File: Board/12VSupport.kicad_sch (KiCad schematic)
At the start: 33 parts, among them J1 12V, J2 BATT, J3 BUCK_IN, J4 BUCK_OUT, J5 BOOST_IN, J6 BOOST_OUT, J8 HEATER, K1 SLA-05VDC-SL-C, K2 SLA-05VDC-SL-C, K3 SLA-05VDC-SL-C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

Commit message: Change fuse holders.
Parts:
- F1, F2: footprint Fuse:Fuseholder_Blade_Mini_Keystone_3568 -> spetry:Fuseholder_Blade
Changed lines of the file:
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@@
 			)
 		)
-		(property "Footprint" "Fuse:Fuseholder_Blade_Mini_Keystone_3568"
+		(property "Footprint" "spetry:Fuseholder_Blade"
 			(at 44.45 154.178 90)
 			(effects
@@
 			)
 		)
-		(property "Footprint" "Fuse:Fuseholder_Blade_Mini_Keystone_3568"
+		(property "Footprint" "spetry:Fuseholder_Blade"
 			(at 54.61 122.682 90)
 			(effects

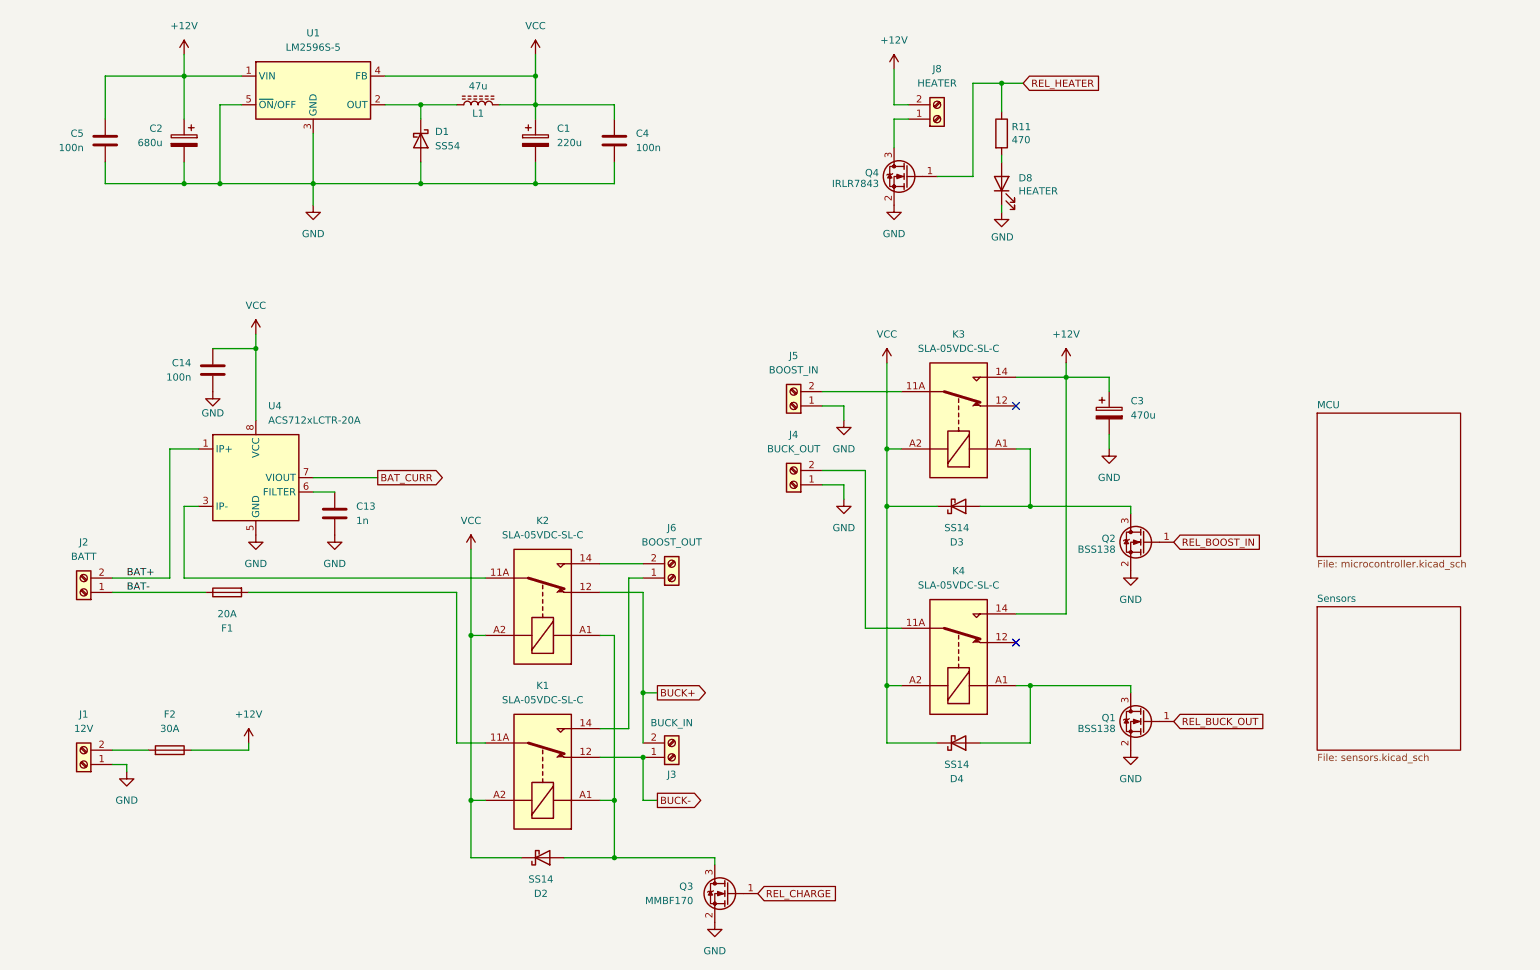
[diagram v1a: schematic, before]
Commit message: Remove diode in MCU supply line so MCU has full 5V.
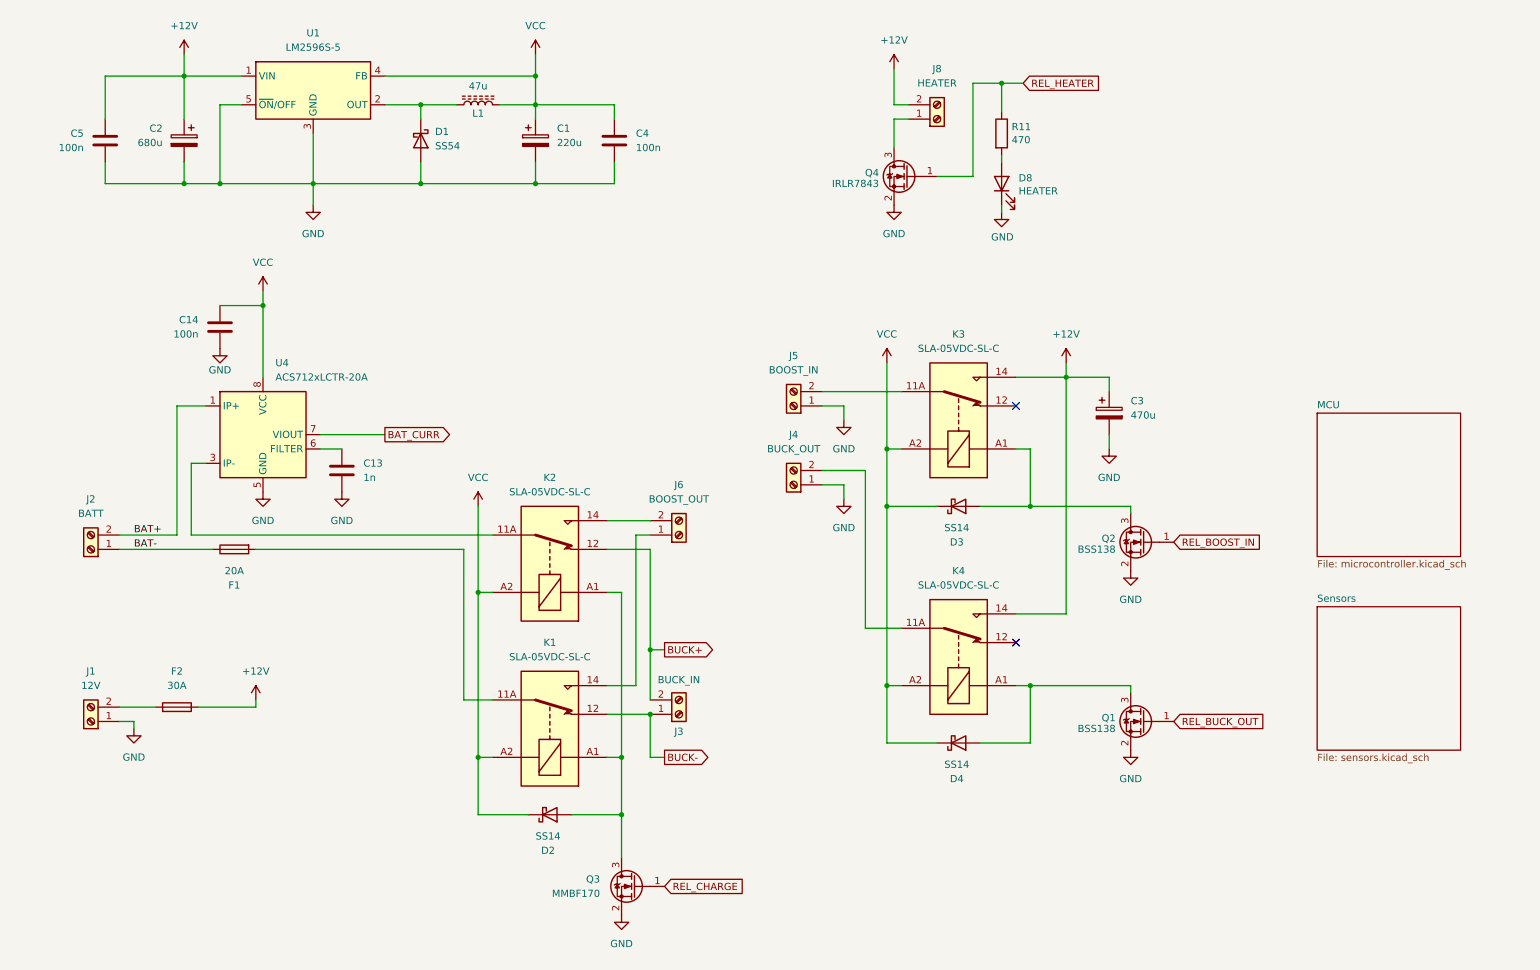
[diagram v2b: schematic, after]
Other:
- moved on the sheet: C13, C14, D2, F1, F2, J1, J2, J3, J6, K1, K2, Q3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

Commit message: Board WIP
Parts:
- F2: value 30A -> 40A
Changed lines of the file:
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@@
 			)
 		)
-		(property "Value" "30A"
+		(property "Value" "40A"
 			(at 45.72 140.97 90)
 			(effects

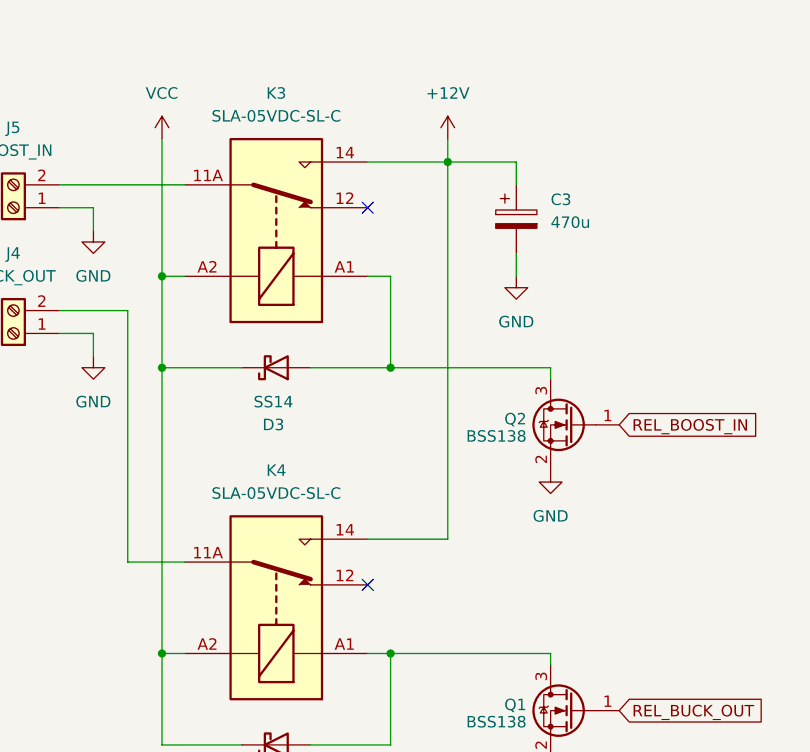
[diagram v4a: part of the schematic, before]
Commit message: Layout improvements. Set version to 1.1
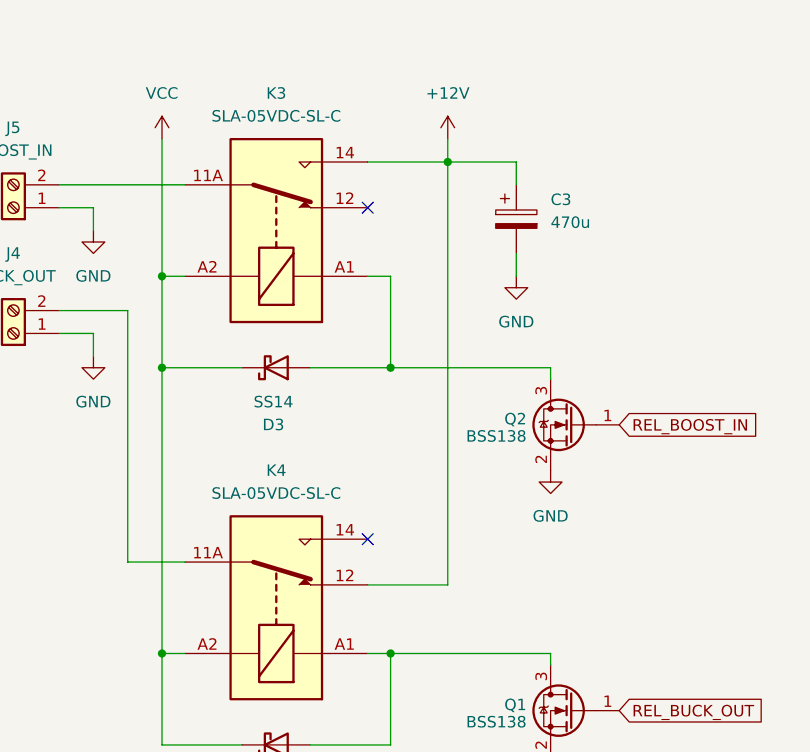
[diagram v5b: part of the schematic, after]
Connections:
- net +12V: now also K4.12; no longer K4.14
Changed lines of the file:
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@@
 	(title_block
 		(date "2024-12-11")
-		(rev "1.0")
+		(rev "1.1")
 	)
 	(junction
@@
 	)
 	(no_connect
-		(at 194.31 133.35)
+		(at 194.31 128.27)
 	)
 	(wire
@@
 	(wire
 		(pts
-			(xy 194.31 128.27) (xy 203.2 128.27)
-		)
-		(stroke
-			(width 0)
-			(type default)
-		)
-	)
-	(wire
-		(pts
 			(xy 123.19 48.26) (xy 123.19 52.07)
 		)
@@
 	(wire
 		(pts
-			(xy 203.2 128.27) (xy 203.2 86.36)
-		)
-		(stroke
-			(width 0)
-			(type default)
-		)
-	)
-	(wire
-		(pts
 			(xy 60.96 73.66) (xy 60.96 86.36)
 		)
@@
 	(wire
 		(pts
+			(xy 203.2 86.36) (xy 203.2 133.35)
+		)
+		(stroke
+			(width 0)
+			(type default)
+		)
+	)
+	(wire
+		(pts
 			(xy 101.6 143.51) (xy 96.52 143.51)
 		)
@@
 		)
 		(stroke
+			(width 0)
+			(type default)
+		)
+	)
+	(wire
+		(pts
+			(xy 203.2 133.35) (xy 194.31 133.35)
+		)
+		(stroke

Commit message: WIP
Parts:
- added Q5: NCE30P30K, Package_TO_SOT_SMD:TO-252-2, symbol Transistor_FET:QM6015D
- added Q6: BSS138, Package_TO_SOT_SMD:SOT-23, symbol Transistor_FET:BSS138
- added R24: 10K, Resistor_SMD:R_0805_2012Metric, symbol Device:R
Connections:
- net +12V: now also Q5.3 (S), R24.2
- net GND: now also Q6.2 (S)
- net BUCK_OUT+: now reaches J4.2 (Pin_2), K4.11A, K4.11B
- net BOOST_IN+: now reaches J5.2 (Pin_2), K3.11A, K3.11B
- net BOOST_IN+: now also Q5.2 (D)
- new net: Q5.1 (G), Q6.3 (D), R24.1
- new net EN_BOOST_IN: Q6.1 (G)
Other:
- moved on the sheet: C13, C14, C3, D2, D8, F1, F2, J1, J2, J3, J4, J5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

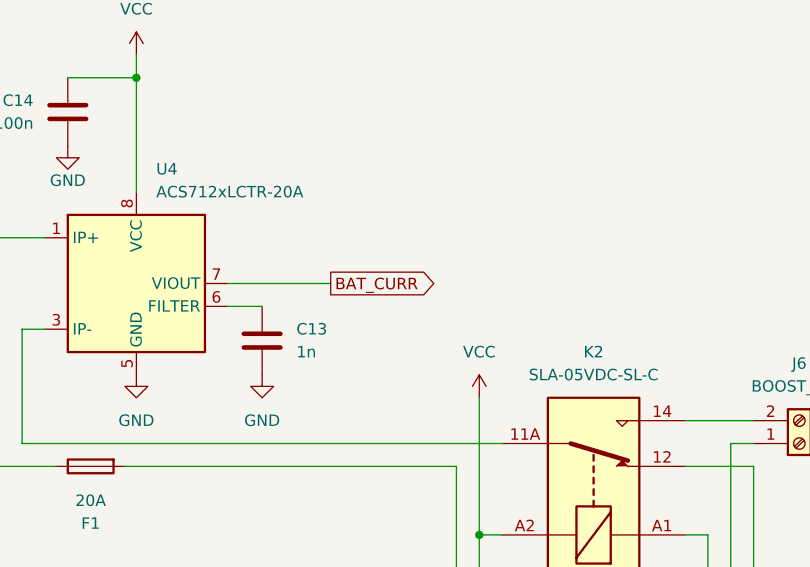
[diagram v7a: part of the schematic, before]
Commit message: Fixes battery voltage sensing.
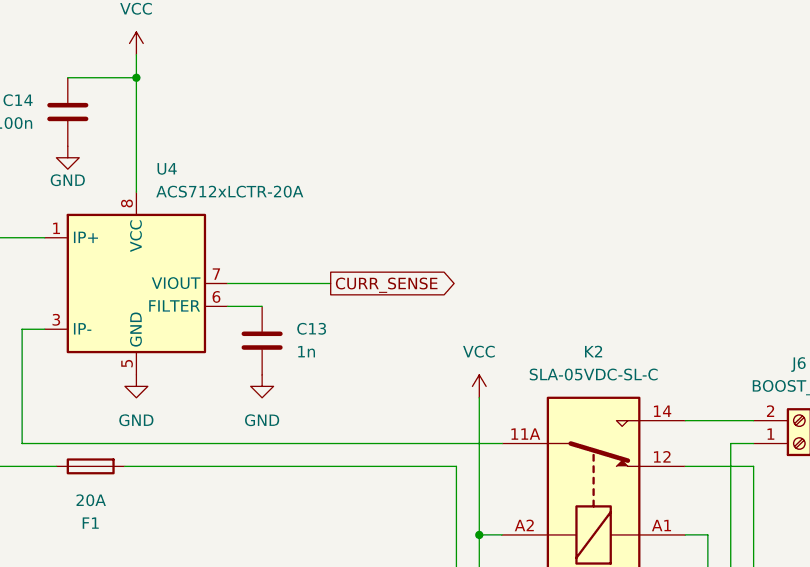
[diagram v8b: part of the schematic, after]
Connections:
- net BAT_CURR renamed CURR_SENSE
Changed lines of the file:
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@@
 		)
 	)
-	(global_label "BAT_CURR"
+	(global_label "CURR_SENSE"
 		(shape output)
 		(at 71.12 96.52 0)
@@
 		)
 		(property "Intersheetrefs" "${INTERSHEET_REFS}"
-			(at 83.5395 96.52 0)
+			(at 86.2608 96.52 0)
 			(effects
 				(font
